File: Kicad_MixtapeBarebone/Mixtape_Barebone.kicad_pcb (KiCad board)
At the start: 2 copper layers, 39.4 x 18.4 mm, 33 parts, among them IC1 ATTINY85-20PU, J1 PB5, J10 S-Out, J11 LED, J2 PB3, J3 PB4, J4 GND, J5 PB0, J6 PB1, J7 PB2, J8 VCC, J9 Prog, SW1 SW_SPST

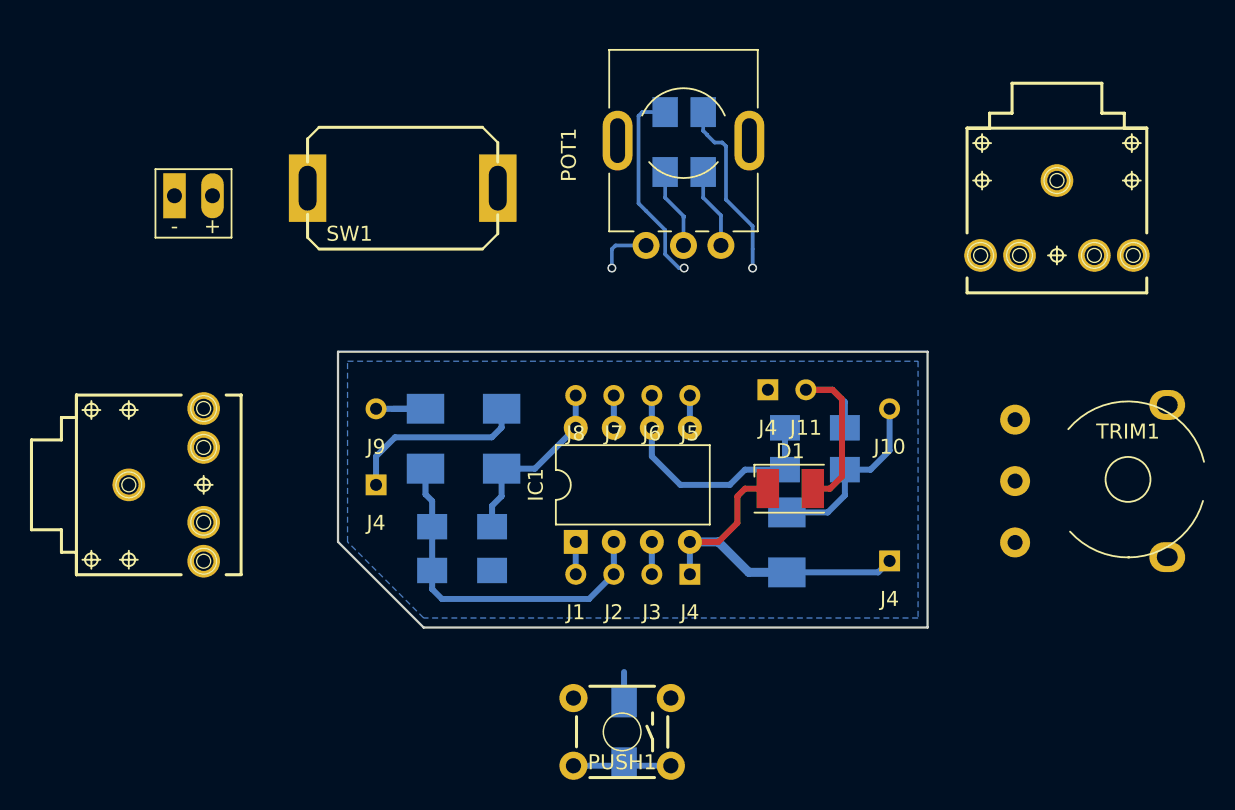
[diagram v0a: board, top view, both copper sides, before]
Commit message: Single Sided DIY version
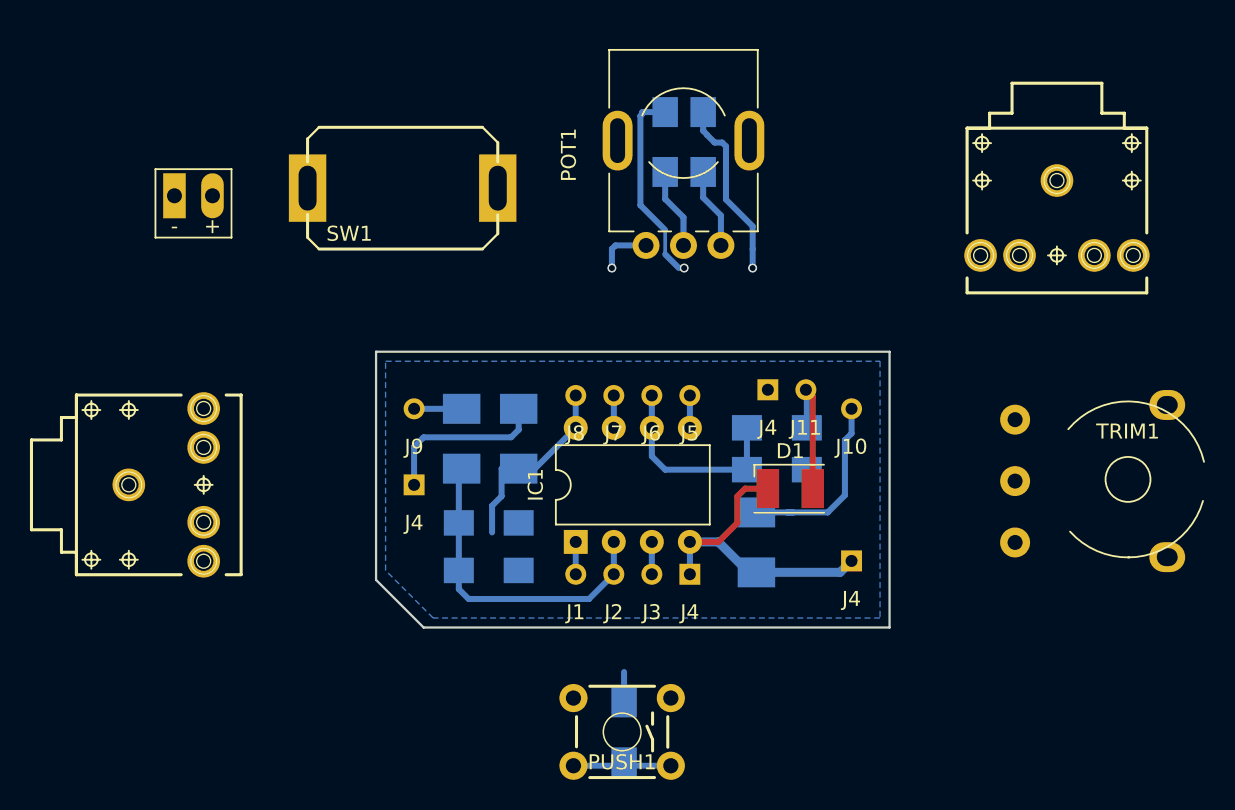
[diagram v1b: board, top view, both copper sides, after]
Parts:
- moved J10 2.54 mm to (101.6, 55.9)
- moved J4 2.54 mm to (72.4, 61.0)
- moved J4 2.54 mm to (101.6, 66.0)
- moved J9 2.54 mm to (72.4, 55.9)
- moved R6 2.54 mm to (96.6, 57.1)
- moved R7 2.54 mm to (96.6, 59.9)
- moved C1 2.41 mm to (75.6, 57.9)
- moved C3 2.03 mm to (95.2, 64.8)
- moved R1 1.80 mm to (77.4, 63.5)
- moved R2 1.78 mm to (77.4, 66.7)
- moved C2 1.14 mm to (79.4, 57.9)
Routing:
- net Net-(D1-Pad2): track 14.8 -> 9.36 mm
- net GND: track 42.2 -> 38.2 mm
- net Net-(IC1-Pad6): track 17.0 -> 13.6 mm
- net Net-(C1-Pad2): track 5.46 -> 3.17 mm
- net Net-(C1-Pad1): track 25.5 -> 23.6 mm
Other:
- board size 39.4 x 18.4 mm -> 34.3 x 18.4 mm

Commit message: Designing the MicroCore Barebone Mixtape
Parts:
- added ?: , 8BitMixtape_DIY-CAD:MicroMixtape_edge, F.Cu at (87.0, 52.1)
- added J3: PB4, 8BitMixtape_DIY-CAD:Loch_mixtape, F.Cu at (72.4, 55.9)
- added J4: GND, 8BitMixtape_DIY-CAD:GND_Loch_mixtape, F.Cu at (77.5, 54.0)
- added J8: VCC, 8BitMixtape_DIY-CAD:Loch_mixtape, F.Cu at (80.0, 54.0)
- IC1: footprint Housings_DIP:DIP-8_W7.62mm -> 8BitMixtape_DIY-CAD:Attiny_DIP-8_W7.62mm
- J1, J2, J3, J5, J6, J7, J8: footprint 8BitMixtape_DIY-CAD:Loch_mixtape -> 8BitMixtape_DIY-CAD:Loch_mixtape_seltsam
- J4: footprint 8BitMixtape_DIY-CAD:GND_Loch_mixtape -> 8BitMixtape_DIY-CAD:Loch_mixtape_seltsam
- moved J4 5.08 mm to (72.4, 66.0)
- moved J9 5.08 mm to (72.4, 61.0)
- moved D1 3.45 mm to (101.0, 61.2), turned to 90 degrees
- moved J11 2.13 mm to (96.5, 54.0)
- moved J4 2.13 mm to (94.0, 54.0)
- moved R4 1.80 mm to (90.4, 36.8)
- moved POT1 1.80 mm to (94.1, 43.7)
- moved R5 1.80 mm to (93.0, 36.8)
- moved C1 1.14 mm to (75.6, 59.0)
- moved C2 1.14 mm to (79.4, 59.0)
- moved R1 0.51 mm to (77.4, 64.0)
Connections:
- net Net-(C1-Pad1) renamed Prog
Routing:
- net Net-(IC1-Pad3): track 2.16 -> 31.5 mm
- net GND: track 38.2 -> 12.0 mm
- net Net-(D1-Pad2): track 9.36 -> 13.8 mm
- net Net-(C1-Pad2): track 3.17 -> 6.37 mm
- net VCC: track 24.8 -> 27.9 mm
- net Net-(C3-Pad2): track 12.8 -> 15.3 mm
- net Prog: track 23.6 -> 23.0 mm
- net Net-(IC1-Pad6): track 13.6 -> 13.0 mm
- added copper zone on F.Cu, net GND
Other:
- board size 34.3 x 18.4 mm -> 35.5 x 23.2 mm

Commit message: mCore Mixtape and more DIY-CAD stuff
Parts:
- removed BAT1: Battery, 8BitMixtape_DIY-CAD:Bat_connector+-
- removed J6: PB1, 8BitMixtape_DIY-CAD:Loch_mixtape_seltsam
- removed POT1: POT, 8BitMixtape_DIY-CAD:Mixtape_Pot_Alps
- removed PUSH1: SW_Push, 8BitMixtape_DIY-CAD:TACTILE-PTH_6mm
- removed R3, R4: 22K, 8BitMixtape_DIY-CAD:R_1206_Mixtape
- removed R5: 4K7, 8BitMixtape_DIY-CAD:R_1206_Mixtape
- removed SW1: SW_SPST, 8BitMixtape_DIY-CAD:Push_SWITCH
- removed TRIM1: POT, 8BitMixtape_DIY-CAD:Potentiometer_wheel
- added J4: GND, 8BitMixtape_DIY-CAD:Loch_mixtape_seltsam, F.Cu at (88.3, 54.5)
- added NEO1: SK6813b, 8BitMixtape_DIY-CAD:Mixtape_NEO_WS2812B, F.Cu at (77.4, 60.9)
- added NEO2: SK6813b, 8BitMixtape_DIY-CAD:Mixtape_NEO_WS2812B, F.Cu at (96.6, 60.9)
- D1: footprint 8BitMixtape_DIY-CAD:LED_2835 -> 8BitMixtape_DIY-CAD:TOP_led_footprint
- JACK1, JACK2: footprint 8BitMixtape_DIY-CAD:AUDIO-Jack_3.5mm_5Pin -> 8BitMixtape_DIY-CAD:AUDIO-JACK-3.5mm_SMD_noPrint
- moved JACK2 28.6 mm to (105.4, 67.4), turned to 90 degrees
- moved JACK1 16.5 mm to (68.6, 67.3), turned to 90 degrees
- moved D1 10.5 mm to (101.2, 50.7), turned to 0 degrees
- moved J10 1.40 mm to (101.6, 57.3)
- moved J4 1.27 mm to (72.4, 64.8)
- moved J3 1.27 mm to (72.4, 57.1)
- moved J4 1.15 mm to (101.7, 64.9)
- moved J5 0.51 mm to (90.8, 54.5)
- moved J7 0.51 mm to (85.7, 54.5)
- moved J8 0.51 mm to (83.2, 54.5)
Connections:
- net Net-(IC1-Pad5) renamed NEO
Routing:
- net Net-(NEO1-Pad2): track 0.00 -> 31.4 mm
- net VCC: track 27.9 -> 53.4 mm, vias 1 -> 0
- net NEO: track 2.25 -> 19.9 mm
- net Net-(IC1-Pad7): track 15.6 -> 5.21 mm, vias 1 -> 0
- net Net-(PUSH1-Pad1): track 6.69 -> 0.00 mm
- net Net-(POT1-Pad2): track 5.41 -> 0.00 mm
- net Net-(POT1-Pad3): track 5.36 -> 0.00 mm, vias 1 -> 0
- net Net-(IC1-Pad6): track 13.0 -> 10.9 mm
- net Prog: track 23.0 -> 21.0 mm
- net GND: track 12.0 -> 13.8 mm
- net Net-(C3-Pad2): track 15.3 -> 13.7 mm
- net Net-(IC1-Pad3): track 31.5 -> 32.8 mm
- net (no net): track 0.00 -> 1.08 mm
- net Net-(D1-Pad2): track 13.8 -> 12.7 mm
